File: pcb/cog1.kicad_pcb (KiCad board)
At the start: 2 copper layers, 115 x 100 mm, 125 parts, among them CN1 VL0631510000G, CN2 VL0831510000G, CN3 VL0831510000G, CN4 VL0831510000G, CN5 VL0831510000G, J1 Conn_01x04_Pin, K1 Relay_SPST-NO, K2 Relay_SPST-NO, K3 Relay_SPST-NO, K4 Relay_SPST-NO, Q1 BC807, Q2 BC807, Q3 BC807, Q4 BC807, Q5 BC807, U1 PCF8523T, U10 MAX13487E, U12 ADC128D818, U2 ISO1212, U3 PCA8574D, U4 ISO1212, U5 AOZ1284PI, Y1 32.768 KHz

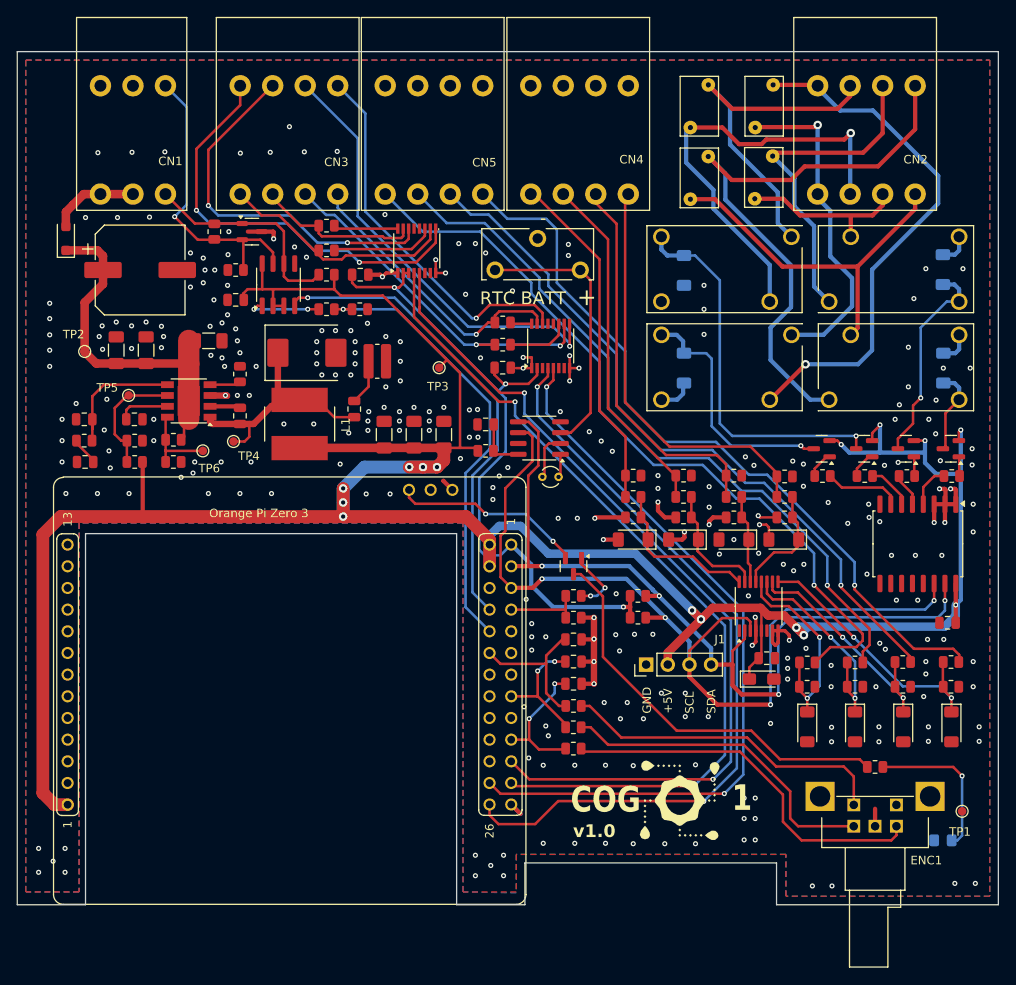
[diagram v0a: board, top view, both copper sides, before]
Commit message: Added recommended threshold resistor and capacitor to all digital inputs, as recommended in the ISO1212 datasheet.
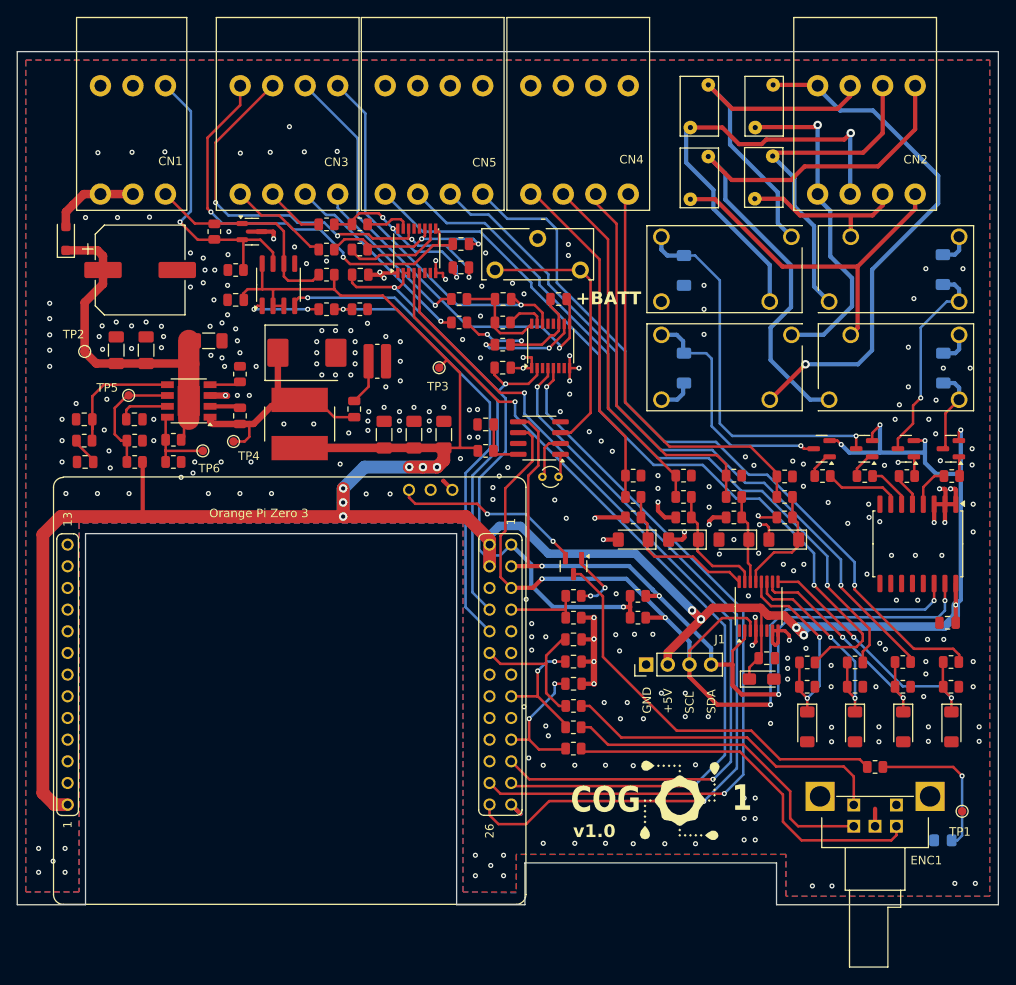
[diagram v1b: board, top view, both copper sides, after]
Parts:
- added C23: 10nF, Capacitor_SMD:C_0805_2012Metric, F.Cu at (151.9, 75.4)
- added C24: 10nF, Capacitor_SMD:C_0805_2012Metric, F.Cu at (158.4, 75.4)
- added C25: 10nF, Capacitor_SMD:C_0805_2012Metric, F.Cu at (147.0, 71.7)
- added C26: 10nF, Capacitor_SMD:C_0805_2012Metric, F.Cu at (147.0, 69.0)
- added R15: 330R, Resistor_SMD:R_0805_2012Metric, F.Cu at (131.2, 66.7)
- added R19: 330R, Resistor_SMD:R_0805_2012Metric, F.Cu at (131.2, 69.6)
- added R22: 330R, Resistor_SMD:R_0805_2012Metric, F.Cu at (146.8, 75.4)
- added R25: 330R, Resistor_SMD:R_0805_2012Metric, F.Cu at (146.8, 78.2)
- moved R5 3.90 mm to (135.2, 66.7)
- moved R6 3.90 mm to (135.2, 69.6), turned to 180 degrees
- turned R49 to 180 degrees
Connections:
- R48 pad 1: DIN1 -> Net-(U4-SENSE1)
- R48 pad 2: Net-(U4-SENSE1) -> Net-(U4-IN1)
- R49 pad 1: DIN2 -> Net-(U4-SENSE2)
- R49 pad 2: Net-(U4-SENSE2) -> Net-(U4-IN2)
- R5 pad 1: DIN3 -> Net-(U2-SENSE1)
- R5 pad 2: Net-(U2-SENSE1) -> Net-(U2-IN1)
- R6 pad 1: DIN4 -> Net-(U2-SENSE2)
- R6 pad 2: Net-(U2-SENSE2) -> Net-(U2-IN2)
- U2 pad 10: DIN4 -> Net-(U2-IN2)
- U2 pad 15: DIN3 -> Net-(U2-IN1)
- U4 pad 10: DIN2 -> Net-(U4-IN2)
- U4 pad 15: DIN1 -> Net-(U4-IN1)
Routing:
- net DIN2: track 42.3 -> 23.4 mm, vias 2 -> 1
- net DIN4: track 27.7 -> 11.8 mm
- net DIN1: track 33.8 -> 20.0 mm
- net Net-(U2-SENSE1): track 7.59 -> 21.0 mm, vias 0 -> 3
- net DIN3: track 19.2 -> 6.98 mm
- net Net-(U4-IN2): track 0.00 -> 12.2 mm, vias 0 -> 2
- net Net-(U2-IN2): track 0.00 -> 11.8 mm
- net Net-(U4-SENSE2): track 7.45 -> 18.2 mm, vias 0 -> 2
- net Net-(U2-SENSE2): track 12.2 -> 21.3 mm, vias 0 -> 2
- net Net-(U4-SENSE1): track 2.55 -> 11.7 mm
- net DIN3B: track 43.9 -> 52.9 mm, vias 2 -> 4
- net Net-(U2-IN1): track 0.00 -> 5.36 mm
- net Net-(U4-IN1): track 0.00 -> 4.57 mm
- net DIN2B: track 51.8 -> 54.5 mm
- net DIN4B: track 49.9 -> 50.8 mm
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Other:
- board text added: "+BATT"
- board text removed: "RTC BATT"

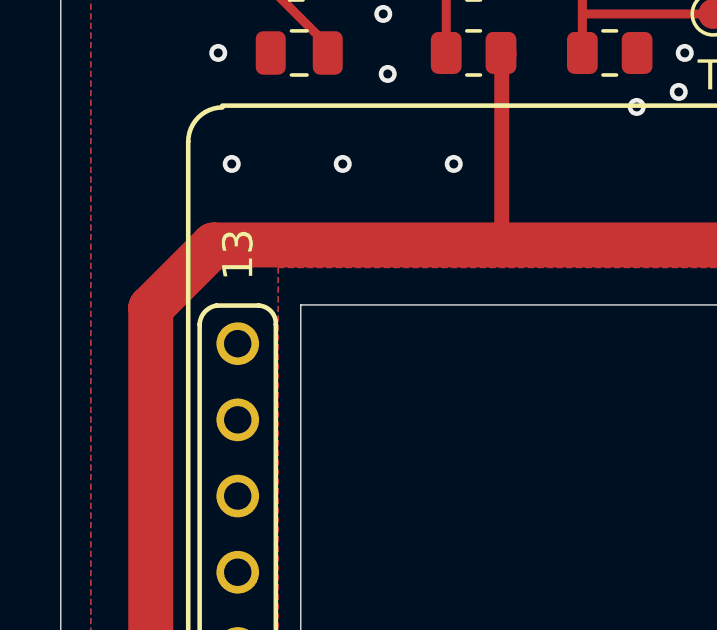
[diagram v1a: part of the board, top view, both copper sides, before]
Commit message: Minor changes in the digital outputs: changed 1K base resistors to 10K to save power. BC807 has an hfe of at least 100.
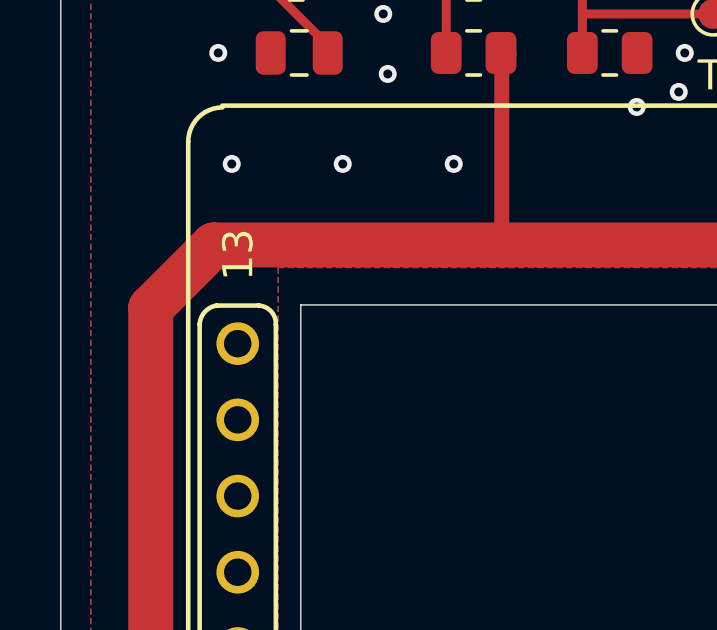
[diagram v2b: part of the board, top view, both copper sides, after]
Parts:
- K1, K2, K3, K4: value Relay_SPST-NO -> PR5-5V-200-1A
- R36, R37, R38, R39: value 1K -> 10K
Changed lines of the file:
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@@
 		(tags "resistor")
 		(property "Reference" "R49"
-			(at 0 -1.65 360)
+			(at 0 -1.65 0)
 			(layer "F.SilkS")
 			(hide yes)
@@
 		)
 		(property "Value" "560R"
-			(at 3.9 -0.1 360)
+			(at 3.9 -0.1 0)
 			(layer "F.Fab")
 			(effects
@@
 			)
 		)
-		(property "Value" "Relay_SPST-NO"
+		(property "Value" "PR5-5V-200-1A"
 			(at 7 -3 180)
 			(unlocked yes)
@@
 		(fp_arc
 			(start 31.75 -51.3)
-			(mid 31.552368 -50.885262)
+			(mid 31.552362 -50.885301)
 			(end 31.12 -50.73)
 			(stroke
@@
 			)
 		)
-		(property "Value" "Relay_SPST-NO"
+		(property "Value" "PR5-5V-200-1A"
 			(at 7 -3 180)
 			(unlocked yes)
@@
 		(tags "resistor")
 		(property "Reference" "R5"
-			(at 0 -1.65 360)
+			(at 0 -1.65 0)
 			(layer "F.SilkS")
 			(hide yes)
@@
 		)
 		(property "Value" "560R"
-			(at 4.05 0 360)
+			(at 4.05 0 0)
 			(layer "F.Fab")
 			(effects
@@
 			)
 		)
-		(property "Value" "1K"
+		(property "Value" "10K"
 			(at 0.0375 -1.65 0)
 			(layer "F.Fab")
@@
 			)
 		)
-		(property "Value" "1K"
+		(property "Value" "10K"
 			(at 0.025 1.65 0)
 			(layer "F.Fab")
@@
 			)
 		)
-		(property "Value" "Relay_SPST-NO"
+		(property "Value" "PR5-5V-200-1A"
 			(at 7 -3 0)
 			(unlocked yes)
@@
 		(tags "resistor")
 		(property "Reference" "R6"
-			(at 0 -1.65 360)
+			(at 0 -1.65 0)
 			(layer "F.SilkS")
 			(hide yes)
@@
 		)
 		(property "Value" "560R"
-			(at 3.95 -0.05 360)
+			(at 3.95 -0.05 0)
 			(layer "F.Fab")
 			(effects
@@
 			)
 		)
-		(property "Value" "1K"
+		(property "Value" "10K"
 			(at -0.1375 1.65 0)
 			(layer "F.Fab")
@@
 			)
 		)
-		(property "Value" "Relay_SPST-NO"
+		(property "Value" "PR5-5V-200-1A"
 			(at 7 -3 0)
 			(unlocked yes)
@@
 			)
 		)
-		(property "Value" "1K"
+		(property "Value" "10K"
 			(at -0.1125 -1.65 0)
 			(layer "F.Fab")

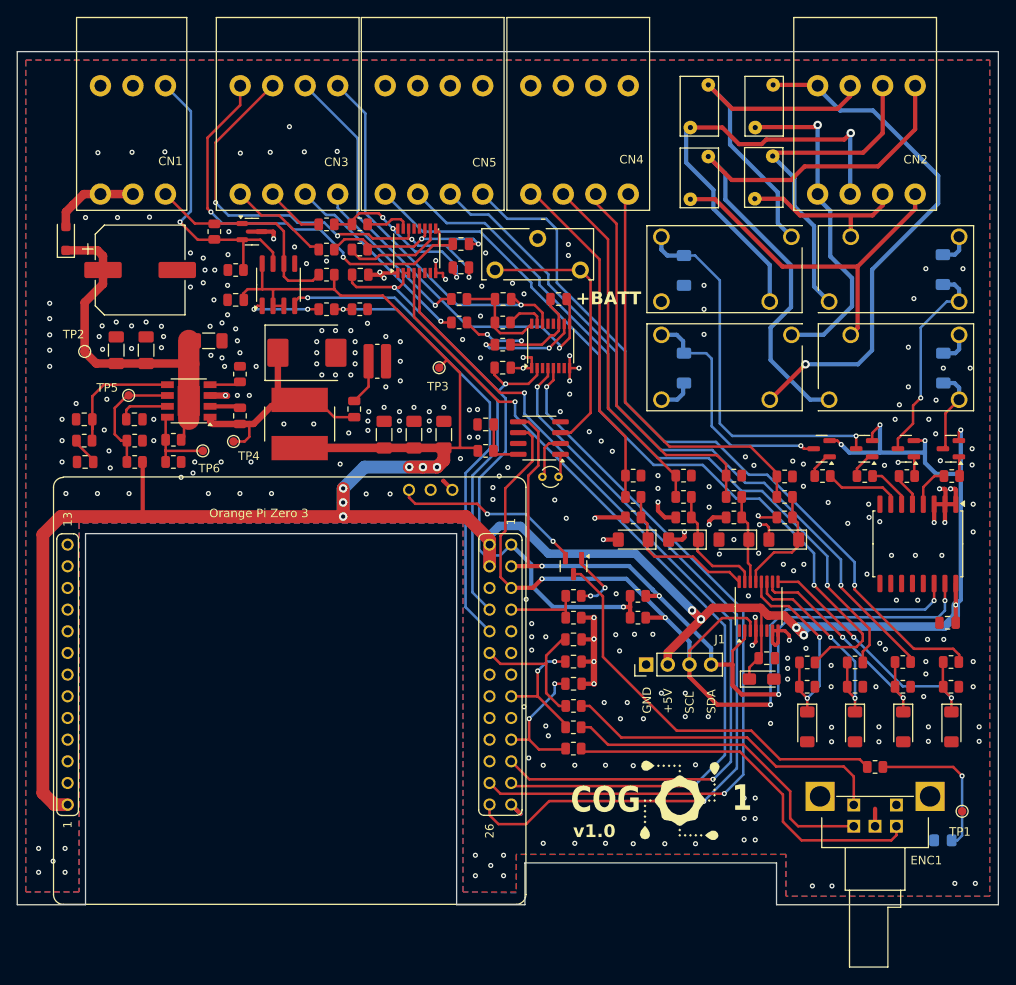
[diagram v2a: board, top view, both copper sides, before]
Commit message: Updated pcb and sent to prototype production as the first official version.
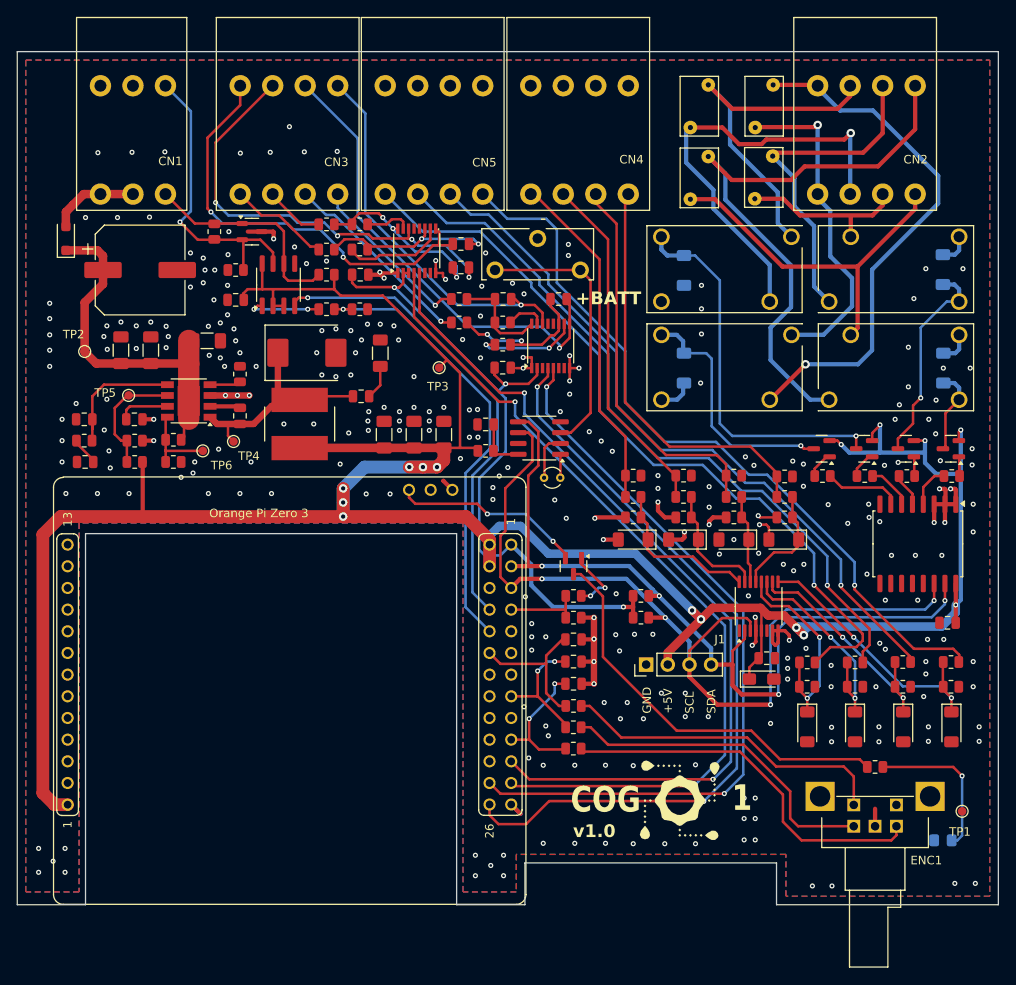
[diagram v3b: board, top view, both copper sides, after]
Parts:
- R59: footprint Resistor_SMD:R_0815_2038Metric_Pad1.20x4.05mm_HandSolder -> Resistor_SMD:R_1206_3216Metric_Pad1.30x1.75mm_HandSolder
- moved C19 1.70 mm to (135.3, 86.8), turned to 180 degrees
- moved R59 1.01 mm to (137.6, 81.8), turned to 90 degrees
- moved C8 0.55 mm to (107.2, 81.4)
- moved C9 0.55 mm to (110.7, 81.4)
- moved R46 0.35 mm to (168.1, 110.2)
- moved R47 0.35 mm to (168.1, 112.8)
- moved Y1 0.22 mm to (158.7, 96.3)
- moved C10 0.19 mm to (117.2, 80.3)
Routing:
- net GND: track 93.8 -> 99.0 mm, vias 289 -> 286
- net Net-(D3-K): track 27.6 -> 25.3 mm
- net Net-(C19-Pad1): track 5.34 -> 4.04 mm
- net Net-(D1-K): track 41.6 -> 42.4 mm
- net SDA: track 96.7 -> 95.9 mm
